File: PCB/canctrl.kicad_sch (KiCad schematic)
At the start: 18 parts, among them U4 SN65HVD230DR, U5 MCP2515-xSO, Y2 ABM8-16.000MHZ-B2-T

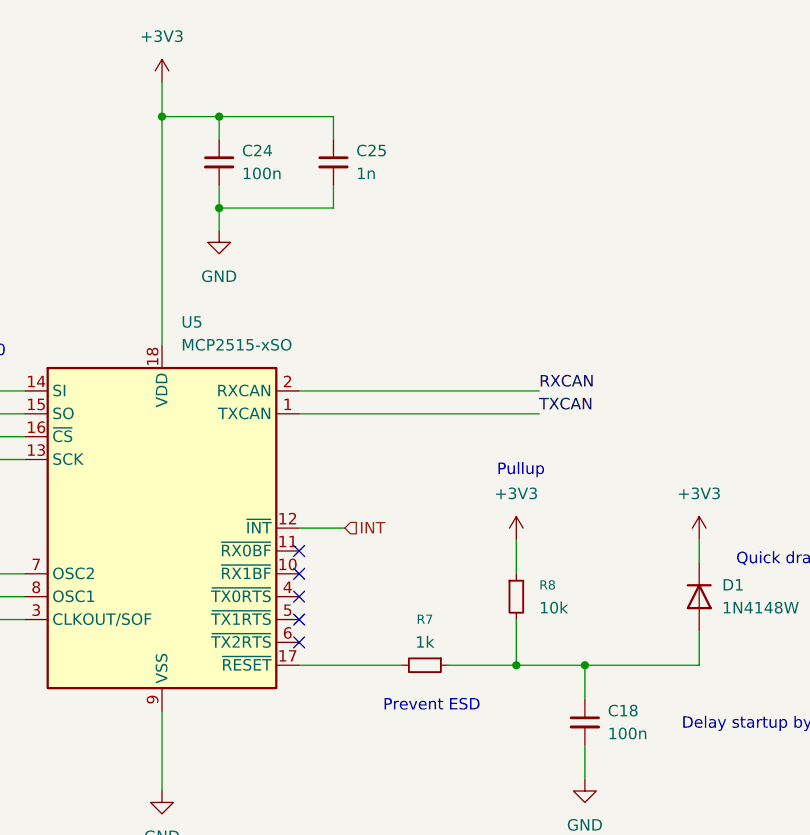
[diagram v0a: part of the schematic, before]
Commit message: PCB routing, better placement
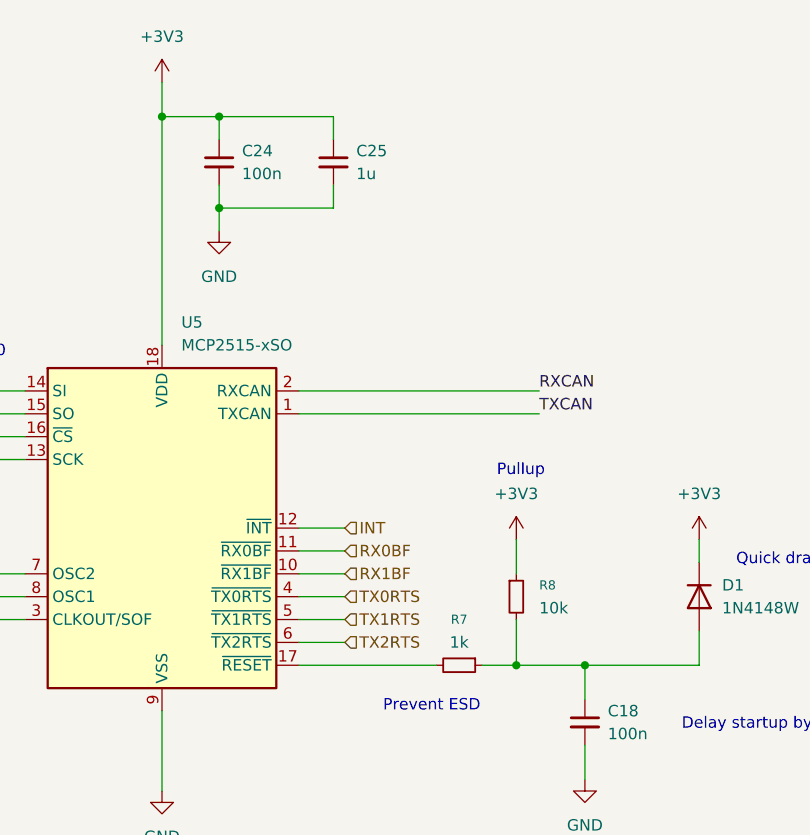
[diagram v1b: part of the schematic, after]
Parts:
- C25: value 1n -> 1u
- Y2: footprint ABM8-16.000MHZ-B2-T-Alt:XTAL_ABM8-16.000MHZ-B2-T -> ABM8-16.000MHZ-B2-T:XTAL_ABM8-16.000MHZ-B2-T
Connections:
- net RX1BF: now reaches U5.10 (~{RX1BF})
- net RX0BF: now reaches U5.11 (~{RX0BF})
- net TX0RTS: now reaches U5.4 (~{TX0RTS})
- net TX1RTS: now reaches U5.5 (~{TX1RTS})
- net TX2RTS: now reaches U5.6 (~{TX2RTS})
- no-connect marks 5 -> 0
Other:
- moved on the sheet: R7
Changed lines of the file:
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@@
 		(color 0 0 0 0)
 	)
-	(no_connect
-		(at 123.19 90.17)
-	)
-	(no_connect
-		(at 123.19 80.01)
-	)
-	(no_connect
-		(at 123.19 87.63)
-	)
-	(no_connect
-		(at 123.19 85.09)
-	)
-	(no_connect
-		(at 123.19 82.55)
-	)
 	(wire
 		(pts
@@
 	(wire
 		(pts
+			(xy 123.19 85.09) (xy 128.27 85.09)
+		)
+		(stroke
+			(width 0)
+			(type default)
+		)
+	)
+	(wire
+		(pts
 			(xy 97.79 171.45) (xy 97.79 179.07)
 		)
@@
 	(wire
 		(pts
+			(xy 123.19 82.55) (xy 128.27 82.55)
+		)
+		(stroke
+			(width 0)
+			(type default)
+		)
+	)
+	(wire
+		(pts
 			(xy 115.57 165.1) (xy 115.57 170.18)
 		)
@@
 	(wire
 		(pts
-			(xy 139.7 92.71) (xy 147.32 92.71)
+			(xy 123.19 80.01) (xy 128.27 80.01)
+		)
+		(stroke
+			(width 0)
+			(type default)
+		)
+	)
+	(wire
+		(pts
+			(xy 143.51 92.71) (xy 147.32 92.71)
 		)
 		(stroke
@@
 	(wire
 		(pts
+			(xy 123.19 87.63) (xy 128.27 87.63)
+		)
+		(stroke
+			(width 0)
+			(type default)
+		)
+	)
+	(wire
+		(pts
 			(xy 123.19 62.23) (xy 149.86 62.23)
 		)
@@
 	(wire
 		(pts
-			(xy 123.19 92.71) (xy 134.62 92.71)
+			(xy 123.19 92.71) (xy 138.43 92.71)
+		)
+		(stroke
+			(width 0)
+			(type default)
+		)
+	)
+	(wire
+		(pts
+			(xy 123.19 90.17) (xy 128.27 90.17)
 		)
 		(stroke
@@
 		)
 	)
+	(hierarchical_label "TX0RTS"
+		(shape input)
+		(at 128.27 85.09 0)
+		(effects
+			(font
+				(size 1.27 1.27)
+			)
+			(justify left)
+		)
+	)
+	(hierarchical_label "RX1BF"
+		(shape input)
+		(at 128.27 82.55 0)
+		(effects
+			(font
+				(size 1.27 1.27)
+			)
+			(justify left)
+		)
+	)
 	(hierarchical_label "CS"
 		(shape input)
@@
 		)
 	)
+	(hierarchical_label "TX2RTS"
+		(shape input)
+		(at 128.27 90.17 0)
+		(effects
+			(font
+				(size 1.27 1.27)
+			)
+			(justify left)
+		)
+	)
+	(hierarchical_label "RX0BF"
+		(shape input)
+		(at 128.27 80.01 0)
+		(effects
+			(font
+				(size 1.27 1.27)
+			)
+			(justify left)
+		)
+	)
 	(hierarchical_label "SI"
 		(shape input)
@@
 			)
 			(justify right)
+		)
+	)
+	(hierarchical_label "TX1RTS"
+		(shape input)
+		(at 128.27 87.63 0)
+		(effects
+			(font
+				(size 1.27 1.27)
+			)
+			(justify left)
 		)
 	)
@@
 	(symbol
 		(lib_id "Device:R_Small")
-		(at 137.16 92.71 270)
+		(at 140.97 92.71 270)
 		(unit 1)
 		(exclude_from_sim no)
@@
 		(fields_autoplaced yes)
 		(property "Reference" "R7"
-			(at 137.16 87.63 90)
+			(at 140.97 87.63 90)
 			(effects
 				(font
@@
 		)
 		(property "Value" "1k"
-			(at 137.16 90.17 90)
+			(at 140.97 90.17 90)
 			(effects
 				(font
@@
 		)
 		(property "Footprint" "Resistor_SMD:R_0603_1608Metric_Pad0.98x0.95mm_HandSolder"
-			(at 137.16 92.71 0)
+			(at 140.97 92.71 0)
 			(effects
 				(font
@@
 		)
 		(property "Datasheet" "~"
-			(at 137.16 92.71 0)
+			(at 140.97 92.71 0)
 			(effects
 				(font
@@
 		)
 		(property "Description" "Resistor, small symbol"
-			(at 137.16 92.71 0)
+			(at 140.97 92.71 0)
 			(effects
 				(font
@@
 			)
 		)
-		(property "Value" "1n"
+		(property "Value" "1u"
 			(at 129.54 38.1062 0)
 			(effects
@@
 			)
 		)
-		(property "Footprint" "ABM8-16.000MHZ-B2-T-Alt:XTAL_ABM8-16.000MHZ-B2-T"
+		(property "Footprint" "ABM8-16.000MHZ-B2-T:XTAL_ABM8-16.000MHZ-B2-T"
 			(at 50.8 86.36 0)
 			(effects
